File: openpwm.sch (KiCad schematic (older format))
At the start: 134 parts, among them J1 Conn_01x04, J10 Conn_01x04, J11 Conn_01x04, J12 Conn_01x04, J13 Conn_01x04, J14 Conn_01x04, J15 Conn_01x04, J16 Conn_01x04, J17 PSU MOLEX 1, J18 PSU MOLEX 2, J19 USB HEADER, J2 Conn_01x04, J20 Cortex Debug Connector, J21 TSENSE_1, J22 TSENSE_2, J23 TSENSE_3, J24 TSENSE_4, J3 Conn_01x04, J4 Conn_01x04, J5 Conn_01x04, J6 Conn_01x04, J7 Conn_01x04, J8 Conn_01x04, J9 Conn_01x04, U1 TPS62111, U2 TM4C123GE6PM, U3 LSF0108, U4 LSF0108, U5 TLP291-4, U6 TLP291-4, U7 TLP291-4, U8 TLP291-4, Y1 Crystal

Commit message: Start the PCB layout
This commit starts the PCB layout. There is still a long way to go;
just using this as checkpoint.
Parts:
- J19: footprint Pin_Headers:Pin_Header_Straight_1x04_Pitch2.00mm -> Pin_Headers:Pin_Header_Straight_1x04_Pitch2.54mm
- Y1: footprint Crystals:Crystal_SMD_HC49-SD_HandSoldering -> Crystals:Crystal_SMD_5032-2pin_5.0x3.2mm_HandSoldering
- renumbered 1uF1 to C20
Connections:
- net +12V: no longer R61.1, R62.1, R63.1, R64.1, R65.1, R66.1, R67.1, R68.1
- net +12VA: now also R61.1, R62.1, R63.1, R64.1, R65.1, R66.1, R67.1, R68.1
- net GND: now also U2.32 (~WAKE~)
- net TSENSE_1: now also U2.64 (AIN4/IDX0/SSI1TX/SSI3TX/WT3CCP1/USB0PFLT/PD3); no longer U2.63 (AIN5/SSI1RX/SSI3RX/WT3CCP0/M0FAULT0/USB0EPEN/PD2)
- net TSENSE_2: now also U2.63 (AIN5/SSI1RX/SSI3RX/WT3CCP0/M0FAULT0/USB0EPEN/PD2); no longer U2.64 (AIN4/IDX0/SSI1TX/SSI3TX/WT3CCP1/USB0PFLT/PD3)
- net TSENSE_3: now also U2.6 (PE3/AIN0); no longer U2.9 (PE0/AIN3/U7RX)
- net TSENSE_4: now also U2.9 (PE0/AIN3/U7RX); no longer U2.6 (PE3/AIN0)
- no-connect marks 8 -> 7

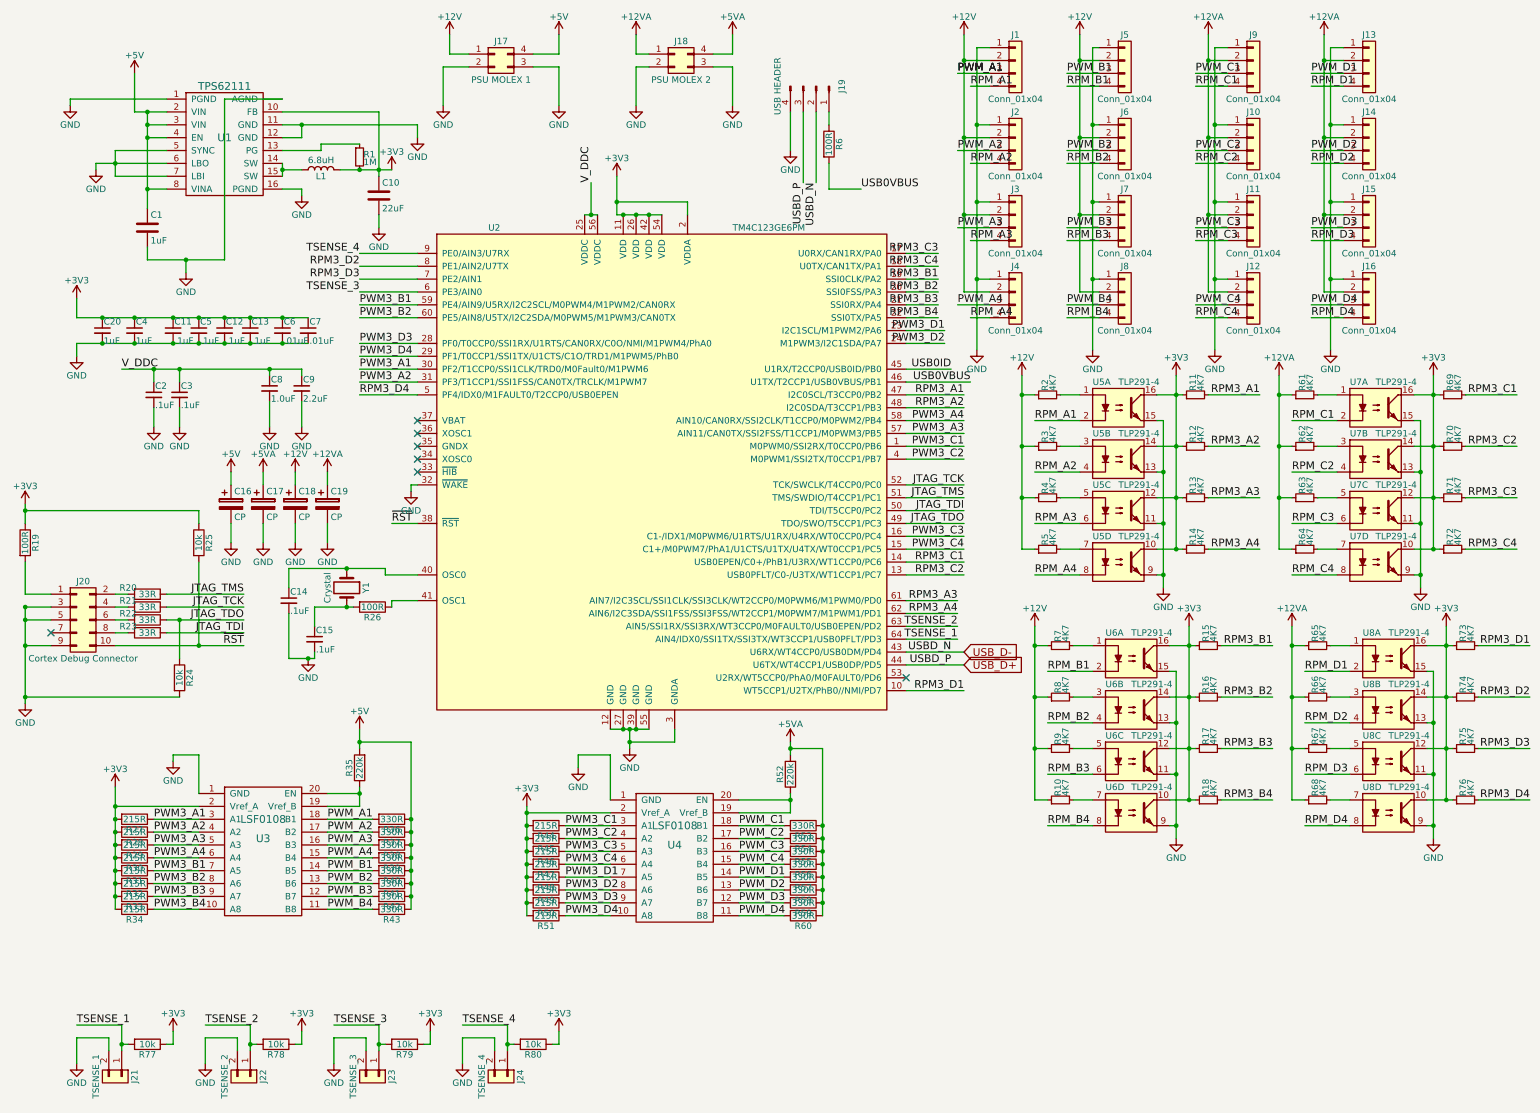
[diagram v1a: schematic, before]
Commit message: Fix optocoupler schematic
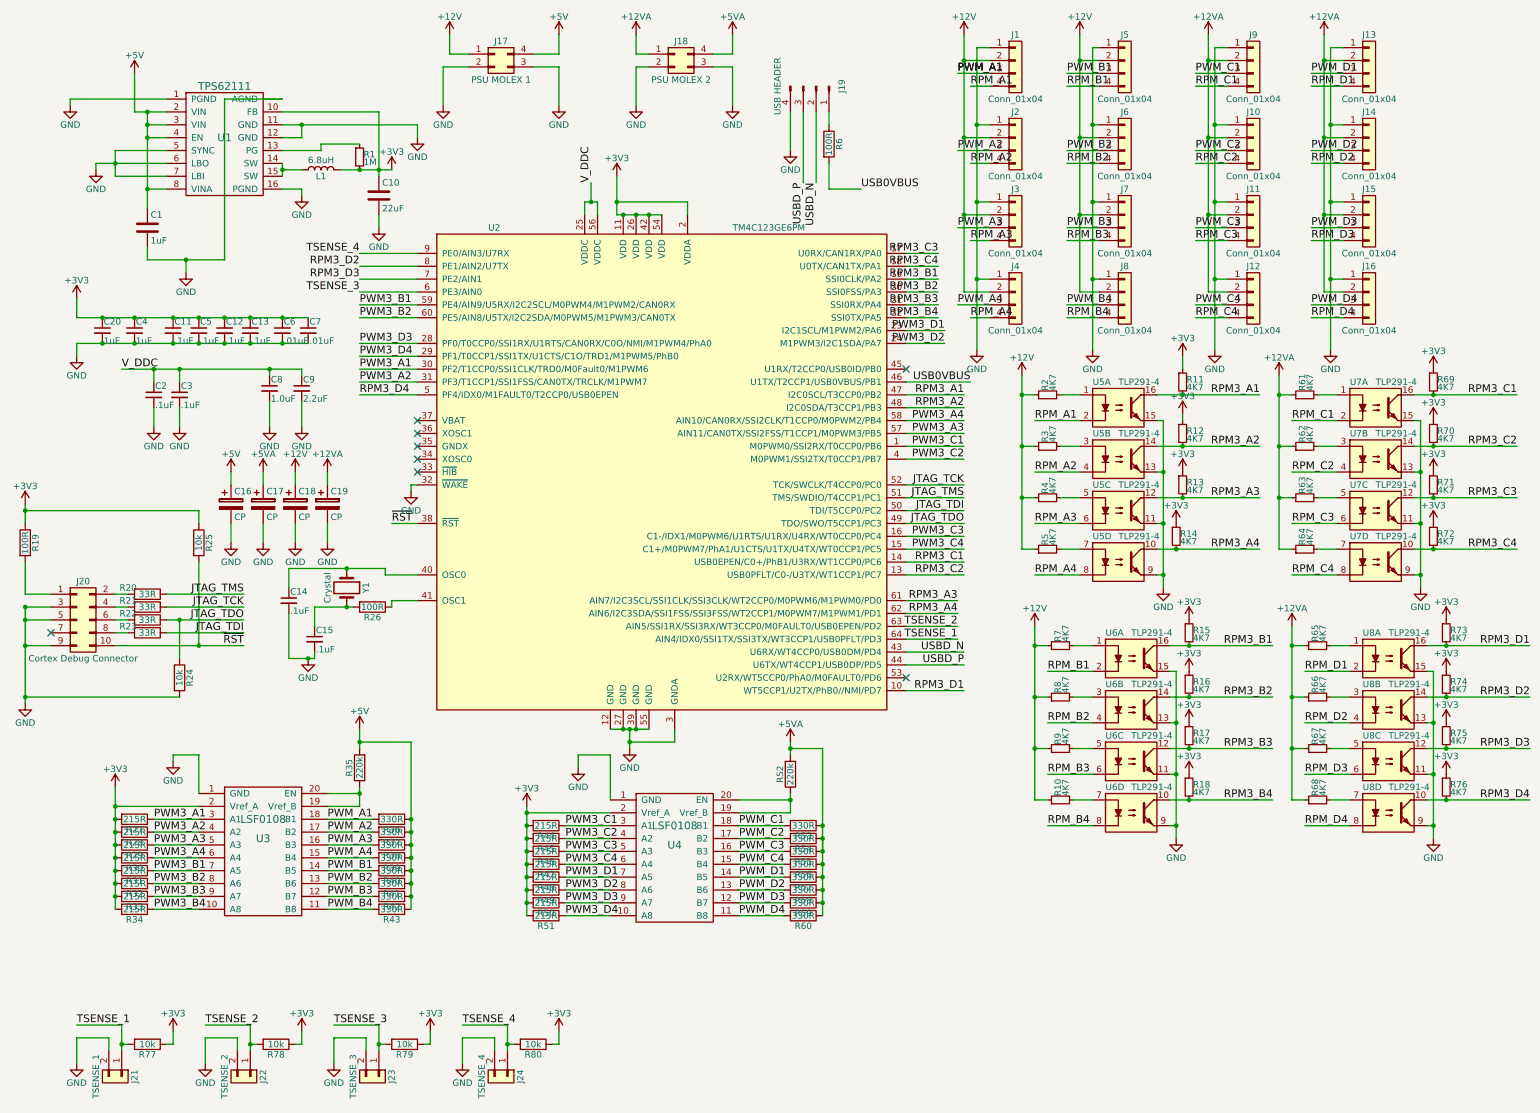
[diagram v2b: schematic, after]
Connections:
- net +3V3: no longer U5.10, U5.12, U5.14, U5.16, U6.10, U6.12, U6.14, U6.16, U7.10, U7.12, U7.14, U7.16, U8.10, U8.12, U8.14, U8.16
- net RPM3_A1: now also U5.16
- net RPM3_A2: now also U5.14
- net RPM3_A3: now also U5.12
- net RPM3_A4: now also U5.10
- net RPM3_B1: now also U6.16
- net RPM3_B2: now also U6.14
- net RPM3_B3: now also U6.12
- net RPM3_B4: now also U6.10
- net RPM3_C1: now also U7.16
- net RPM3_C2: now also U7.14
- net RPM3_C3: now also U7.12
- net RPM3_C4: now also U7.10
- net RPM3_D1: now also U8.16
- net RPM3_D2: now also U8.14
- net RPM3_D3: now also U8.12
- net RPM3_D4: now also U8.10
- net USB0ID: no longer names the net of U2.45 (U1RX/T2CCP0/USB0ID/PB0)
- net USB_D+ renamed USBD_P
- net USB_D- renamed USBD_N
- no-connect marks 7 -> 8
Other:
- moved on the sheet: R11, R12, R13, R14, R15, R16, R17, R18, R69, R70, R71, R72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
